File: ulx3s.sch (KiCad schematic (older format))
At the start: 4 parts, among them U1 LFE5U-25F-6BG381C, U2 ESP-12E

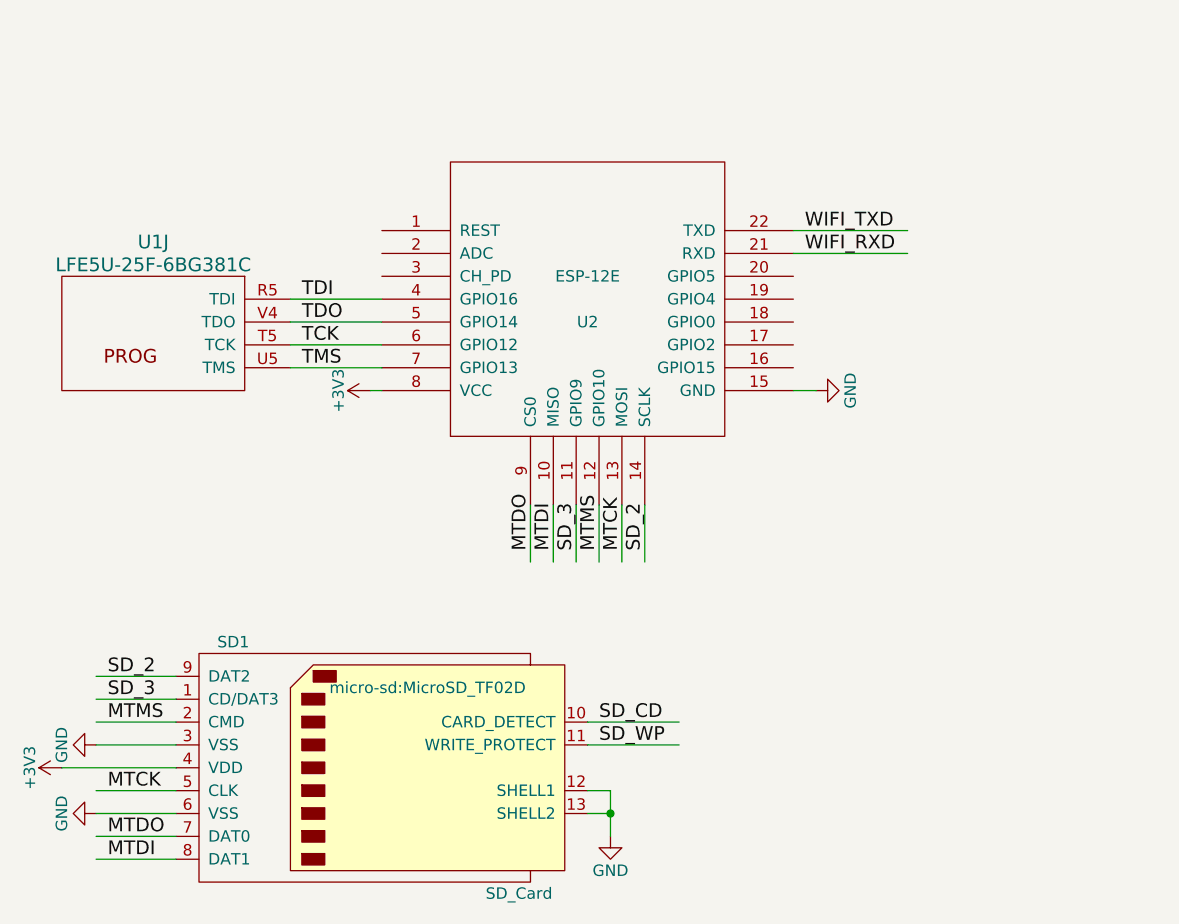
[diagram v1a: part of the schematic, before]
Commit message: add RTC to power sheet Moving wifi to separate sheet
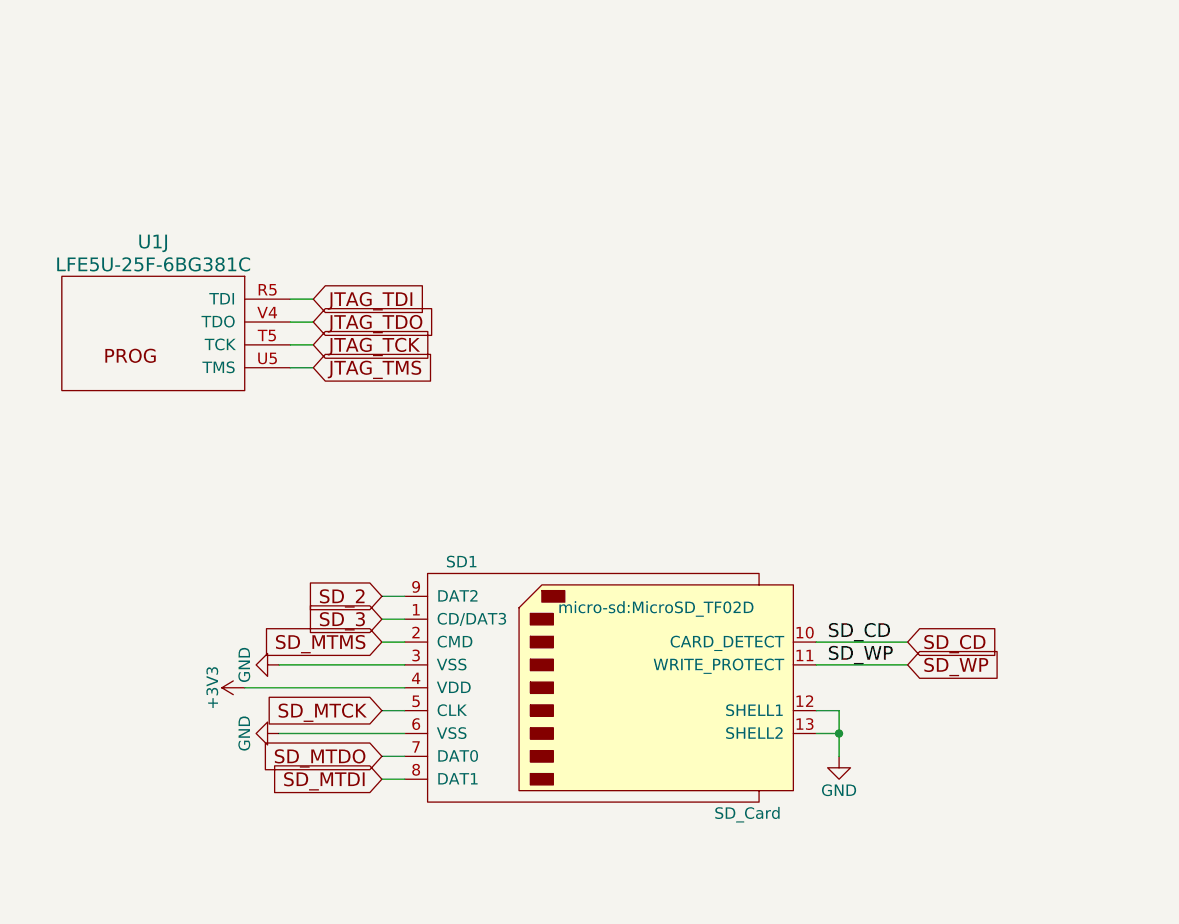
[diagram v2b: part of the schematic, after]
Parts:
- removed U2: ESP-12E, ESP8266:ESP-12E, symbol ESP-12E
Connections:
- net labels added: JTAG_TCK, JTAG_TDI, JTAG_TDO, JTAG_TMS, SD_MTCK, SD_MTDI, SD_MTDO, SD_MTMS
- net labels removed: MTCK, MTDI, MTDO, MTMS, TCK, TDI, TDO, TMS, WIFI_RXD, WIFI_TXD
- wire segments 28 -> 18
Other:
- moved on the sheet: SD1
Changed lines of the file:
@@
 Comment4 ""
 $EndDescr
-$Comp
-L ESP-12E U2
-U 1 1 56AC980A
-P 3200 4550
-F 0 "U2" H 3200 4450 50  0000 C CNN
-F 1 "ESP-12E" H 3200 4650 50  0000 C CNN
-F 2 "ESP8266:ESP-12E" H 3200 4550 50  0001 C CNN
-F 3 "" H 3200 4550 50  0001 C CNN
-	1    3200 4550
-	1    0    0    -1
-$EndComp
 Wire Wire Line
-	2300 4650 1900 4650
-Text Label 1950 4650 0    60   ~ 0
-TDO
+	2000 4650 1900 4650
 Wire Wire Line
-	2300 4550 1900 4550
-Text Label 1950 4550 0    60   ~ 0
-TDI
+	2000 4550 1900 4550
 Wire Wire Line
-	1900 4750 2300 4750
-Text Label 1950 4750 0    60   ~ 0
-TCK
-Wire Wire Line
-	1900 4850 2300 4850
-Text Label 1950 4850 0    60   ~ 0
-TMS
-Wire Wire Line
-	4100 4950 4200 4950
-$Comp
-L GND #PWR01
-U 1 1 56ACA1D2
-P 4200 4950
-F 0 "#PWR01" H 4200 4700 50  0001 C CNN
-F 1 "GND" H 4200 4800 50  0000 C CNN
-F 2 "" H 4200 4950 60  0000 C CNN
-F 3 "" H 4200 4950 60  0000 C CNN
-	1    4200 4950
-	0    -1   -1   0
-$EndComp
+	1900 4850 2000 4850
 $Comp
 L SD_Card SD1
 U 1 1 56ACBF19
-P 2300 6600
-F 0 "SD1" H 1650 7150 50  0000 C CNN
-F 1 "SD_Card" H 2900 6050 50  0000 C CNN
-F 2 "micro-sd:MicroSD_TF02D" H 2500 6950 50  0000 C CNN
-F 3 "" H 2300 6600 60  0000 C CNN
-	1    2300 6600
+P 3300 6250
+F 0 "SD1" H 2650 6800 50  0000 C CNN
+F 1 "SD_Card" H 3900 5700 50  0000 C CNN
+F 2 "micro-sd:MicroSD_TF02D" H 3500 6600 50  0000 C CNN
+F 3 "" H 3300 6250 60  0000 C CNN
+	1    3300 6250
 	1    0    0    -1
 $EndComp
@@
 $EndComp
 Wire Wire Line
-	2950 5450 2950 5700
-Text Label 2950 5650 1    60   ~ 0
-MTDO
+	2400 5850 2300 5850
 Wire Wire Line
-	3050 5450 3050 5700
+	2300 5950 2400 5950
 Wire Wire Line
-	3150 5450 3150 5700
+	2300 6050 2400 6050
 Wire Wire Line
-	3250 5450 3250 5700
+	2400 6350 2300 6350
 Wire Wire Line
-	3350 5450 3350 5700
+	2300 6550 2400 6550
 Wire Wire Line
-	3450 5450 3450 5700
-Text Label 3050 5650 1    60   ~ 0
-MTDI
-Text Label 3150 5650 1    60   ~ 0
-SD_3
-Text Label 3250 5650 1    60   ~ 0
-MTMS
-Text Label 3350 5650 1    60   ~ 0
-MTCK
-Text Label 3450 5650 1    60   ~ 0
-SD_2
-Wire Wire Line
-	1400 6200 1050 6200
-Text Label 1100 6200 0    60   ~ 0
-SD_2
-Wire Wire Line
-	1050 6300 1400 6300
-Text Label 1100 6300 0    60   ~ 0
-SD_3
-Wire Wire Line
-	1050 6400 1400 6400
-Text Label 1100 6400 0    60   ~ 0
-MTMS
-Wire Wire Line
-	1400 6700 1050 6700
-Text Label 1100 6700 0    60   ~ 0
-MTCK
-Wire Wire Line
-	1050 6900 1400 6900
-Text Label 1100 6900 0    60   ~ 0
-MTDO
-Wire Wire Line
-	1050 7000 1400 7000
-Text Label 1100 7000 0    60   ~ 0
-MTDI
+	2300 6650 2400 6650
 $Sheet
 S 7000 5250 750  450
@@
 $EndSheet
 Wire Wire Line
-	2250 4950 2300 4950
+	1850 6150 2400 6150
 Wire Wire Line
-	4100 4250 4600 4250
-Text Label 4150 4250 0    60   ~ 0
-WIFI_TXD
+	1700 6250 2400 6250
 Wire Wire Line
-	4100 4350 4600 4350
-Text Label 4150 4350 0    60   ~ 0
-WIFI_RXD
-Wire Wire Line
-	1050 6500 1400 6500
-Wire Wire Line
-	900  6600 1400 6600
-Wire Wire Line
-	1050 6800 1400 6800
+	1850 6450 2400 6450
 $Comp
-L GND #PWR02
+L GND #PWR01
 U 1 1 58D58197
-P 1050 6500
-F 0 "#PWR02" H 1050 6250 50  0001 C CNN
-F 1 "GND" H 1050 6350 50  0000 C CNN
-F 2 "" H 1050 6500 50  0000 C CNN
-F 3 "" H 1050 6500 50  0000 C CNN
-	1    1050 6500
+P 1850 6150
+F 0 "#PWR01" H 1850 5900 50  0001 C CNN
+F 1 "GND" H 1850 6000 50  0000 C CNN
+F 2 "" H 1850 6150 50  0000 C CNN
+F 3 "" H 1850 6150 50  0000 C CNN
+	1    1850 6150
 	0    1    1    0
 $EndComp
 $Comp
-L GND #PWR03
+L GND #PWR02
 U 1 1 58D581BF
-P 1050 6800
-F 0 "#PWR03" H 1050 6550 50  0001 C CNN
-F 1 "GND" H 1050 6650 50  0000 C CNN
-F 2 "" H 1050 6800 50  0000 C CNN
-F 3 "" H 1050 6800 50  0000 C CNN
-	1    1050 6800
+P 1850 6450
+F 0 "#PWR02" H 1850 6200 50  0001 C CNN
+F 1 "GND" H 1850 6300 50  0000 C CNN
+F 2 "" H 1850 6450 50  0000 C CNN
+F 3 "" H 1850 6450 50  0000 C CNN
+	1    1850 6450
 	0    1    1    0
 $EndComp
 Wire Wire Line
-	3200 6400 3600 6400
-Text Label 3250 6400 0    60   ~ 0
+	4200 6050 4600 6050
+Text Label 4250 6050 0    60   ~ 0
 SD_CD
 Wire Wire Line
-	3200 6500 3600 6500
-Text Label 3250 6500 0    60   ~ 0
+	4200 6150 4600 6150
+Text Label 4250 6150 0    60   ~ 0
 SD_WP
 $Comp
-L GND #PWR04
+L GND #PWR03
 U 1 1 58D58733
-P 3300 6900
-F 0 "#PWR04" H 3300 6650 50  0001 C CNN
-F 1 "GND" H 3300 6750 50  0000 C CNN
-F 2 "" H 3300 6900 50  0000 C CNN
-F 3 "" H 3300 6900 50  0000 C CNN
-	1    3300 6900
+P 4300 6550
+F 0 "#PWR03" H 4300 6300 50  0001 C CNN
+F 1 "GND" H 4300 6400 50  0000 C CNN
+F 2 "" H 4300 6550 50  0000 C CNN
+F 3 "" H 4300 6550 50  0000 C CNN
+	1    4300 6550
 	1    0    0    -1
 $EndComp
 Wire Wire Line
-	3200 6700 3300 6700
+	4200 6350 4300 6350
 Wire Wire Line
-	3300 6700 3300 6900
+	4300 6350 4300 6550
 Wire Wire Line
-	3200 6800 3300 6800
-Connection ~ 3300 6800
+	4200 6450 4300 6450
+Connection ~ 4300 6450
 $Comp
-L +3V3 #PWR05
-U 1 1 58D5F08C
-P 2250 4950
-F 0 "#PWR05" H 2250 4800 50  0001 C CNN
-F 1 "+3V3" H 2250 5090 50  0000 C CNN
-F 2 "" H 2250 4950 50  0000 C CNN
-F 3 "" H 2250 4950 50  0000 C CNN
-	1    2250 4950
-	0    -1   -1   0
-$EndComp
-$Comp
-L +3V3 #PWR06
+L +3V3 #PWR04
 U 1 1 58D5F123
-P 900 6600
-F 0 "#PWR06" H 900 6450 50  0001 C CNN
-F 1 "+3V3" H 900 6740 50  0000 C CNN
-F 2 "" H 900 6600 50  0000 C CNN
-F 3 "" H 900 6600 50  0000 C CNN
-	1    900  6600
+P 1700 6250
+F 0 "#PWR04" H 1700 6100 50  0001 C CNN
+F 1 "+3V3" H 1700 6390 50  0000 C CNN
+F 2 "" H 1700 6250 50  0000 C CNN
+F 3 "" H 1700 6250 50  0000 C CNN
+	1    1700 6250
 	0    -1   -1   0
 $EndComp
@@
 F1 "ram.sch" 60
 $EndSheet
+Text GLabel 2000 4550 2    60   Input ~ 0
+JTAG_TDI
+Text GLabel 2000 4650 2    60   Input ~ 0
+JTAG_TDO
+Text GLabel 2000 4750 2    60   Input ~ 0
+JTAG_TCK
+Text GLabel 2000 4850 2    60   Input ~ 0
+JTAG_TMS
+Wire Wire Line
+	1900 4750 2000 4750
+Text GLabel 2300 5850 0    60   Input ~ 0
+SD_2
+Text GLabel 2300 5950 0    60   Input ~ 0
+SD_3
+Text GLabel 2300 6050 0    60   Input ~ 0
+SD_MTMS
+Text GLabel 2300 6350 0    60   Input ~ 0
+SD_MTCK
+Text GLabel 2300 6550 0    60   Input ~ 0
+SD_MTDO
+Text GLabel 2300 6650 0    60   Input ~ 0
+SD_MTDI
+Text GLabel 4600 6050 2    60   Input ~ 0
+SD_CD
+Text GLabel 4600 6150 2    60   Input ~ 0
+SD_WP
 $EndSCHEMATC

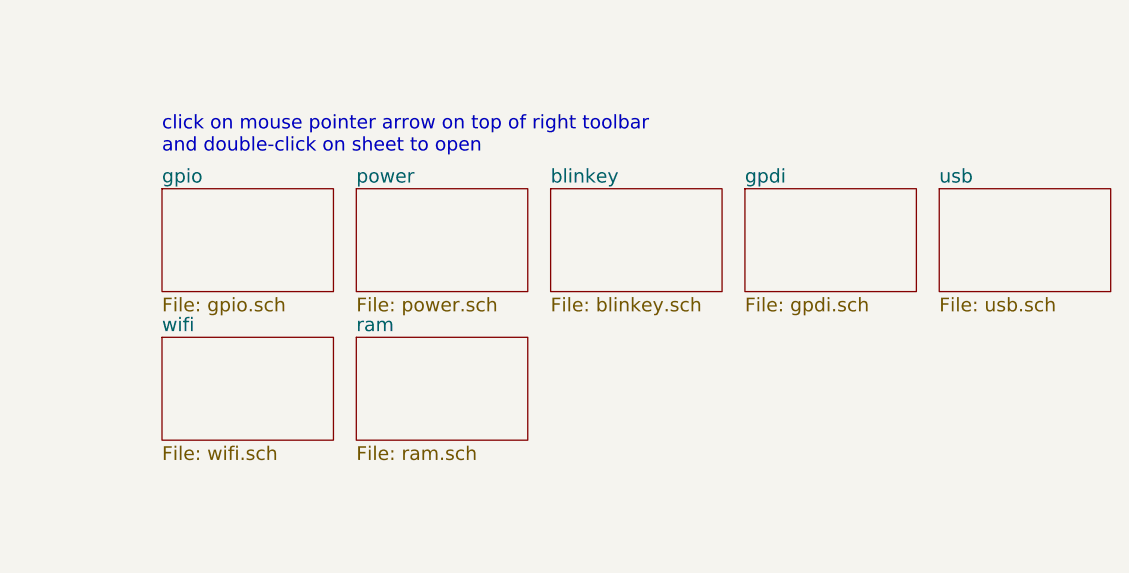
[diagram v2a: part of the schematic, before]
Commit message: Add wake on RTC and shutdown network
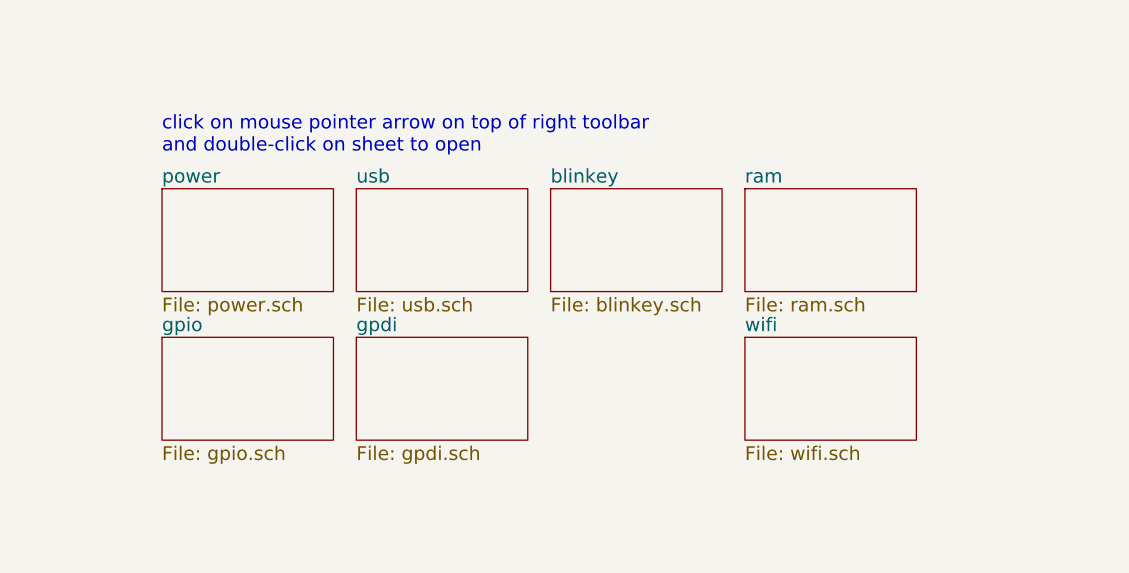
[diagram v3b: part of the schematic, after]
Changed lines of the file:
@@
 	2300 6650 2400 6650
 $Sheet
-S 7000 5250 750  450
+S 7000 5900 750  450
 U 56AC389C
 F0 "gpio" 60
@@
 $EndSheet
 $Sheet
-S 7850 5250 750  450
+S 7000 5250 750  450
 U 58D51CAD
 F0 "power" 60
@@
 click on mouse pointer arrow on top of right toolbar\nand double-click on sheet to open
 $Sheet
-S 9550 5250 750  450
+S 7850 5900 750  450
 U 58D686D9
 F0 "gpdi" 60
@@
 $EndSheet
 $Sheet
-S 10400 5250 750  450
+S 7850 5250 750  450
 U 58D6BF46
 F0 "usb" 60
@@
 $EndSheet
 $Sheet
-S 7000 5900 750  450
+S 9550 5900 750  450
 U 58D6D447
 F0 "wifi" 60
@@
 $EndSheet
 $Sheet
-S 7850 5900 750  450
+S 9550 5250 750  450
 U 58D6D507
 F0 "ram" 60

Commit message: add audio jack footprint
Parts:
- AUDIO1: footprint Pin_Headers:Pin_Header_Angled_2x03 -> audio-jack:CUI_SJ-43516-SMT
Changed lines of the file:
@@
 F 0 "AUDIO1" H 1300 3050 50  0000 C CNN
 F 1 "JACK_TRS_6PINS" H 1250 2350 50  0000 C CNN
-F 2 "Pin_Headers:Pin_Header_Angled_2x03" H 1400 2500 60  0001 C CNN
+F 2 "audio-jack:CUI_SJ-43516-SMT" H 1400 2500 60  0001 C CNN
 F 3 "" H 1400 2500 60  0000 C CNN
 	1    1300 2650

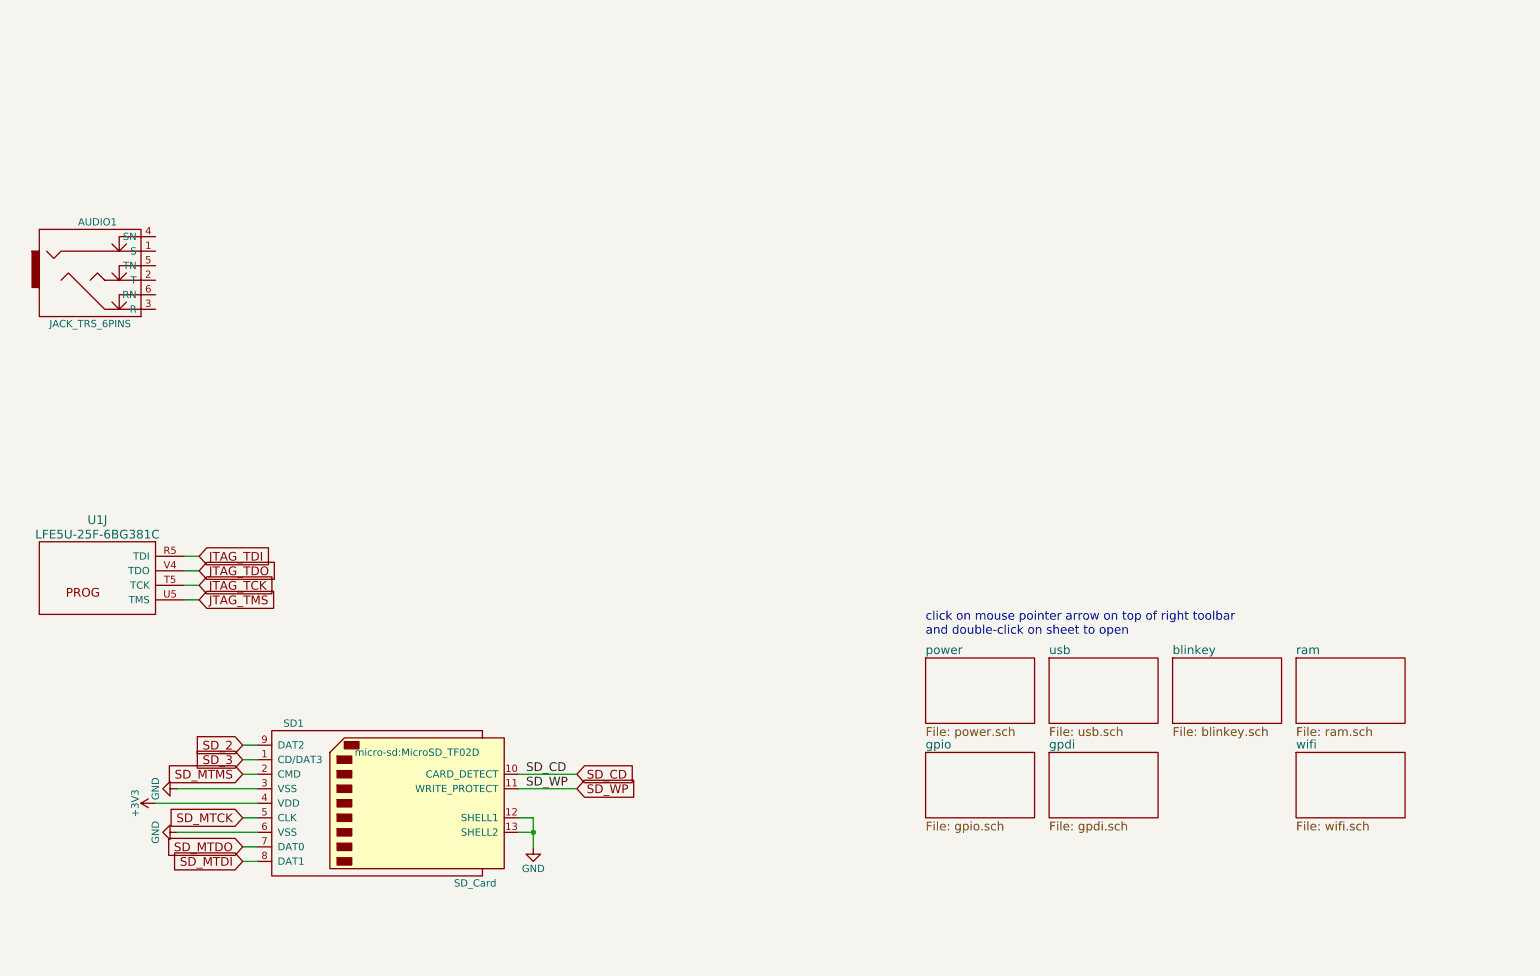
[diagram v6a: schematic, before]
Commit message: audio jack to "analog" sheet
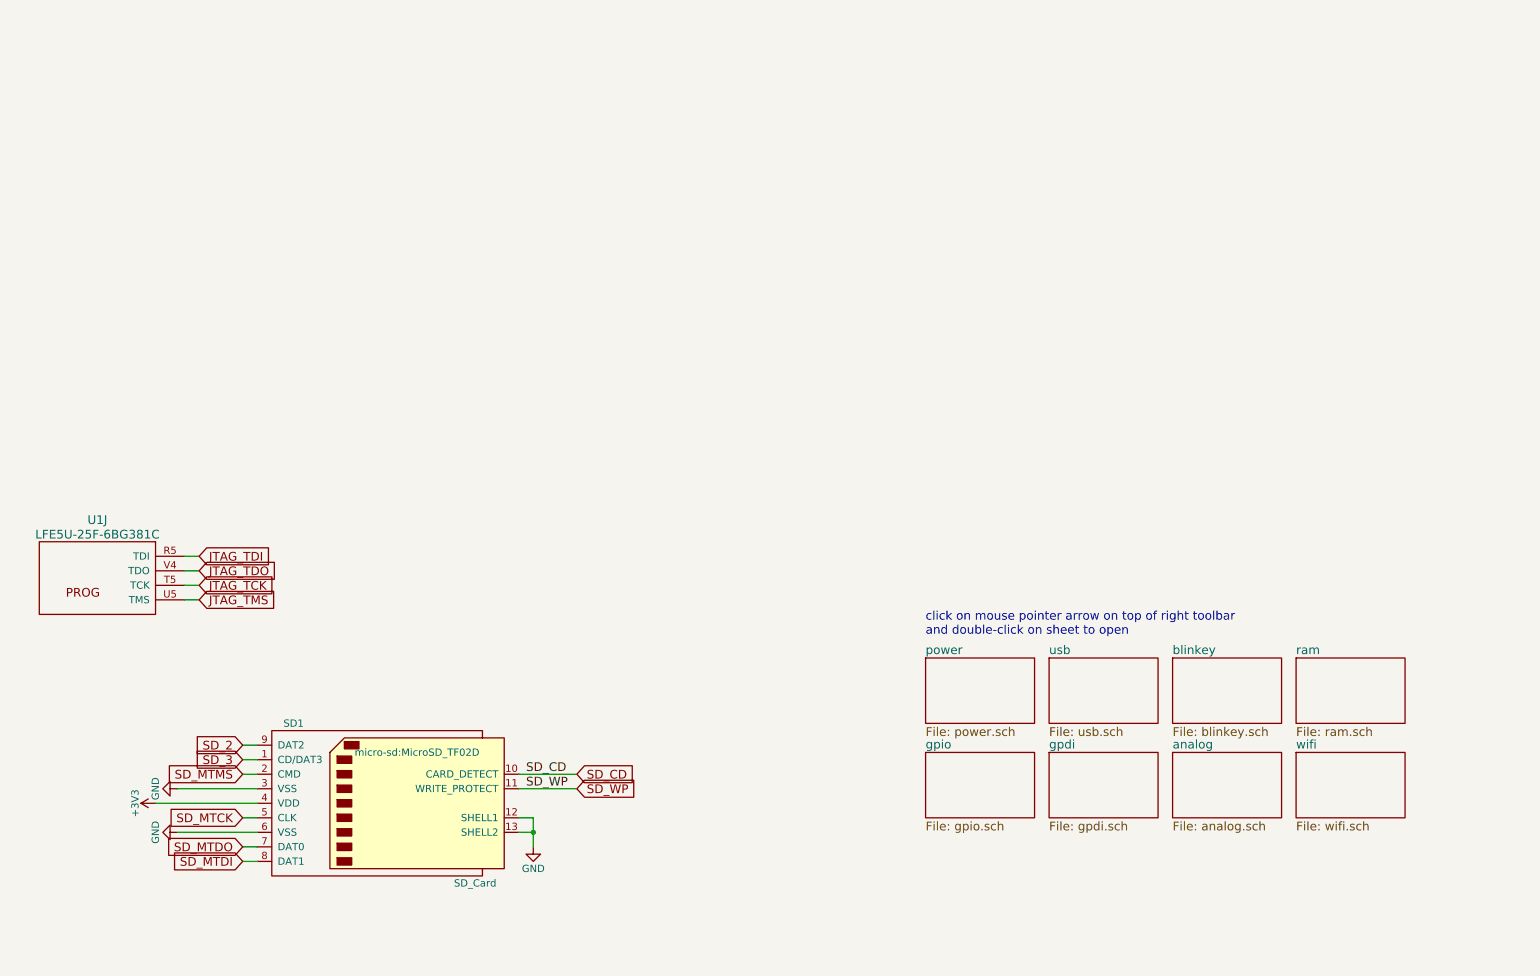
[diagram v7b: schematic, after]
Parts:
- removed AUDIO1: JACK_TRS_6PINS, audio-jack:CUI_SJ-43516-SMT, symbol JACK_TRS_6PINS
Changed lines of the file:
@@
 $Descr A4 11693 8268
 encoding utf-8
-Sheet 1 8
+Sheet 1 9
 Title "ULX3S"
 Date ""
@@
 F 3 "" H 3300 6250 60  0000 C CNN
 	1    3300 6250
-	1    0    0    -1
-$EndComp
-$Comp
-L JACK_TRS_6PINS AUDIO1
-U 1 1 56A9D95B
-P 1300 2650
-F 0 "AUDIO1" H 1300 3050 50  0000 C CNN
-F 1 "JACK_TRS_6PINS" H 1250 2350 50  0000 C CNN
-F 2 "audio-jack:CUI_SJ-43516-SMT" H 1400 2500 60  0001 C CNN
-F 3 "" H 1400 2500 60  0000 C CNN
-	1    1300 2650
 	1    0    0    -1
 $EndComp
@@
 Text GLabel 4600 6150 2    60   Input ~ 0
 SD_WP
+$Sheet
+S 8700 5900 750  450
+U 58D82BD0
+F0 "analog" 60
+F1 "analog.sch" 60
+$EndSheet
 $EndSCHEMATC
